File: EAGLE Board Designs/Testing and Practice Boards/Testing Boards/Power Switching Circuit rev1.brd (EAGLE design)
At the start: 93.2 x 66.3 mm, 50 parts, among them K1 J115F11A6*, Q1 SIR638ADP, Q2 SIR638ADP, Q3 SIR638ADP, Q4 SIR638ADP, U1 LTC4421, X1 CONNECTOR-3, X100 CONNECTOR-4AUTOSPORT, X101 CONNECTOR-4AUTOSPORT

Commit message: Add files via upload
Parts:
- Q1, Q2, Q3, Q4: device HyTechDevices:SO-8-POWERPAK -> HyTechDevices:POWERPAK_SO-8
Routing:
- net DCDC: track 43.7 -> 39.7 mm, vias 1 -> 0
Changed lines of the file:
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@@
 <drawing>
 <settings>
-<setting alwaysvectorfont="no"/>
+<setting alwaysvectorfont="yes"/>
 <setting verticaltext="up"/>
 </settings>
@@
 Power Switching Board rev1
 By: Sathya Gummadi</text>
-<text x="-15.748" y="32.131" size="0.9144" layer="21" font="vector" ratio="18">DCDC</text>
+<text x="-17.272" y="29.337" size="0.9144" layer="21" font="vector" ratio="18">DCDC</text>
 <text x="53.721" y="25.654" size="0.9144" layer="21" font="vector" ratio="18">GLVB</text>
 <text x="46.101" y="31.623" size="0.9144" layer="21" font="vector" ratio="18">OUT</text>
@@
 <attribute name="NAME" x="39.116" y="9.652" size="0.762" layer="21" font="vector"/>
 </element>
-<element name="Q4" library="HyTechDevices" package="SO-8-POWERPAK" value="SIR638ADP" x="29.718" y="-6.604" smashed="yes" rot="R270">
+<element name="Q4" library="HyTechDevices" package="POWERPAK_SO-8" value="SIR638ADP" x="29.718" y="-6.604" smashed="yes" rot="R270">
+<attribute name="MPN" value="SIR638ADP" x="29.718" y="-6.604" size="1.778" layer="27" rot="R270" display="off"/>
 <attribute name="NAME" x="32.385" y="-6.731" size="0.8128" layer="25" font="vector" rot="R270" align="bottom-center"/>
 </element>
-<element name="Q3" library="HyTechDevices" package="SO-8-POWERPAK" value="SIR638ADP" x="30.734" y="1.524" smashed="yes" rot="R90">
+<element name="Q3" library="HyTechDevices" package="POWERPAK_SO-8" value="SIR638ADP" x="30.734" y="1.524" smashed="yes" rot="R90">
+<attribute name="MPN" value="SIR638ADP" x="30.734" y="1.524" size="1.778" layer="27" rot="R90" display="off"/>
 <attribute name="NAME" x="24.638" y="1.524" size="0.762" layer="25" font="vector" rot="R90" align="bottom-center"/>
 </element>
-<element name="Q1" library="HyTechDevices" package="SO-8-POWERPAK" value="SIR638ADP" x="-3.048" y="25.273" smashed="yes" rot="R180">
-<attribute name="NAME" x="-3.048" y="29.591" size="0.762" layer="25" font="vector" rot="R180" align="bottom-center"/>
-</element>
-<element name="Q2" library="HyTechDevices" package="SO-8-POWERPAK" value="SIR638ADP" x="4.699" y="24.384" smashed="yes">
+<element name="Q1" library="HyTechDevices" package="POWERPAK_SO-8" value="SIR638ADP" x="-3.048" y="25.273" smashed="yes" rot="R180">
+<attribute name="MPN" value="SIR638ADP" x="-3.048" y="25.273" size="1.778" layer="27" rot="R180" display="off"/>
+<attribute name="NAME" x="-3.048" y="30.099" size="0.762" layer="25" font="vector" rot="R180" align="bottom-center"/>
+</element>
+<element name="Q2" library="HyTechDevices" package="POWERPAK_SO-8" value="SIR638ADP" x="4.699" y="24.384" smashed="yes">
+<attribute name="MPN" value="SIR638ADP" x="4.699" y="24.384" size="1.778" layer="27" display="off"/>
 <attribute name="NAME" x="2.667" y="27.686" size="0.762" layer="25" font="vector" align="bottom-center"/>
 </element>
@@
 <contactref element="K1" pad="CONTACT1"/>
 <polygon width="0.1524" layer="1" orphans="yes" thermals="no">
-<vertex x="44.577" y="21.844"/>
-<vertex x="50.673" y="26.797"/>
-<vertex x="53.34" y="26.797"/>
-<vertex x="53.34" y="11.049"/>
-<vertex x="60.071" y="-3.937" curve="-163.432311"/>
-<vertex x="54.220009375" y="-7.66035625"/>
-<vertex x="45.105534375" y="10.5686"/>
+<vertex x="44.45" y="21.59"/>
+<vertex x="50.8" y="26.67" curve="-133.114058"/>
+<vertex x="52.959" y="25.527"/>
+<vertex x="52.959" y="13.843"/>
+<vertex x="59.436" y="-3.683" curve="-176.962356"/>
+<vertex x="53.721" y="-5.969"/>
+<vertex x="42.418" y="15.748" curve="-79.752562"/>
+<vertex x="43.561" y="20.955" curve="-4.410509"/>
 </polygon>
 </signal>
@@
 <contactref element="D1" pad="3"/>
 <wire x1="-9.144" y1="21.908628125" x2="-9.144" y2="16.51" width="1.016" layer="1"/>
-<wire x1="-9.144" y1="21.908628125" x2="-12.49219375" y2="21.908628125" width="1.016" layer="16"/>
-<wire x1="-12.49219375" y1="21.908628125" x2="-12.5897625" y2="22.3659625" width="1.016" layer="16"/>
 <wire x1="-4.826" y1="15.884" x2="-8.518" y2="15.884" width="1.016" layer="1"/>
 <wire x1="-8.518" y1="15.884" x2="-9.144" y2="16.51" width="1.016" layer="1"/>
@@
 <wire x1="5.56790625" y1="11.595146875" x2="5.56790625" y2="11.91790625" width="0.4064" layer="1"/>
 <wire x1="5.56790625" y1="11.91790625" x2="6.223" y2="12.573" width="0.4064" layer="1"/>
-<wire x1="-3.8608" y1="25.4" x2="-3.8608" y2="22.6568" width="0.4064" layer="1"/>
+<wire x1="-3.7338" y1="25.273" x2="-3.8608" y2="22.6568" width="0.4064" layer="1"/>
 <wire x1="-3.8608" y1="22.6568" x2="6.223" y2="12.573" width="0.4064" layer="1"/>
 <wire x1="-9.144" y1="16.51" x2="-9.144" y2="13.1953" width="1.016" layer="1"/>
-<via x="-9.144" y="21.908628125" extent="1-16" drill="0.35"/>
 <contactref element="X101" pad="1"/>
 <polygon width="0.1524" layer="1" orphans="yes" thermals="no">
@@
 <vertex x="36.576" y="16.764"/>
 <vertex x="48.253365625" y="26.126934375" curve="137.037485"/>
-<vertex x="46.744759375" y="30.988"/>
-<vertex x="19.304" y="30.988"/>
+<vertex x="46.784171875" y="30.861"/>
 </polygon>
 </signal>
@@
 <contactref element="Q3" pad="4"/>
 <contactref element="U1" pad="31"/>
-<wire x1="32.766" y1="-1.016" x2="33.02" y2="-1.27" width="0.4064" layer="1"/>
+<wire x1="32.639" y1="-1.143" x2="33.02" y2="-1.27" width="0.4064" layer="1"/>
 <wire x1="33.02" y1="-1.27" x2="33.02" y2="-2.413" width="0.4064" layer="1"/>
 <via x="33.02" y="-2.413" extent="1-16" drill="0.35"/>
@@
 <via x="26.67" y="-3.302" extent="1-16" drill="0.35"/>
 <wire x1="26.67" y1="-3.302" x2="27.432" y2="-4.064" width="0.4064" layer="1"/>
-<wire x1="27.432" y1="-4.064" x2="27.686" y2="-4.064" width="0.4064" layer="1"/>
+<wire x1="27.432" y1="-4.064" x2="27.813" y2="-3.937" width="0.4064" layer="1"/>
 <wire x1="32.639" y1="-2.794" x2="27.178" y2="-2.794" width="0.4064" layer="16"/>
 <wire x1="26.67" y1="-3.302" x2="25.6708625" y2="-3.302" width="0.4064" layer="1"/>
@@
 </polygon>
 <wire x1="13.725771875" y1="4.3808" x2="14.61005625" y2="3.496515625" width="0.4064" layer="1"/>
-<wire x1="25.789028125" y1="-1.016" x2="30.226" y2="-1.016" width="0.4064" layer="1"/>
+<wire x1="25.789028125" y1="-1.016" x2="30.099" y2="-1.143" width="0.4064" layer="1"/>
 <wire x1="14.61005625" y1="3.496515625" x2="21.072275" y2="3.496515625" width="0.4064" layer="1"/>
 <wire x1="21.072275" y1="3.496515625" x2="21.17439375" y2="3.598634375" width="0.4064" layer="1"/>
@@
 <vertex x="26.924" y="-11.684"/>
 </polygon>
-<wire x1="29.591" y1="-7.4168" x2="27.9318" y2="-9.076" width="1.016" layer="1"/>
+<wire x1="29.718" y1="-7.2898" x2="27.9318" y2="-9.076" width="1.016" layer="1"/>
 <wire x1="24.13" y1="-8.246" x2="29.836" y2="-8.246" width="1.016" layer="1"/>
 <wire x1="29.836" y1="-8.246" x2="30.48" y2="-8.89" width="1.016" layer="1"/>
@@
 <wire x1="7.493" y1="13.8598625" x2="6.460553125" y2="14.892309375" width="0.4064" layer="1"/>
 <wire x1="7.493" y1="9.694334375" x2="7.493" y2="13.8598625" width="0.4064" layer="1"/>
-<wire x1="-0.508" y1="27.305" x2="0.762" y2="27.305" width="0.4064" layer="1"/>
-<via x="0.762" y="27.305" extent="1-16" drill="0.35"/>
-<wire x1="0.762" y1="27.305" x2="1.397" y2="26.67" width="0.4064" layer="16"/>
-<wire x1="1.397" y1="26.67" x2="1.397" y2="21.844" width="0.4064" layer="16"/>
+<via x="0.889" y="27.432" extent="1-16" drill="0.35"/>
+<wire x1="0.889" y1="27.432" x2="1.397" y2="26.924" width="0.4064" layer="16"/>
+<wire x1="1.397" y1="26.924" x2="1.397" y2="21.844" width="0.4064" layer="16"/>
 <wire x1="2.032" y1="21.209" x2="2.032" y2="20.828" width="0.4064" layer="16"/>
 <wire x1="2.032" y1="21.209" x2="1.397" y2="21.844" width="0.4064" layer="16"/>
@@
 <wire x1="2.54" y1="18.923" x2="6.460553125" y2="15.002446875" width="0.4064" layer="1"/>
 <wire x1="6.460553125" y1="15.002446875" x2="6.460553125" y2="14.892309375" width="0.4064" layer="1"/>
-<wire x1="2.159" y1="22.352" x2="2.159" y2="20.955" width="0.4064" layer="1"/>
-<wire x1="2.159" y1="20.955" x2="2.032" y2="20.828" width="0.4064" layer="1"/>
+<wire x1="2.032" y1="20.828" x2="2.032" y2="22.479" width="0.4064" layer="1"/>
+<wire x1="-0.381" y1="27.178" x2="-0.127" y2="27.432" width="0.4064" layer="1"/>
+<wire x1="-0.127" y1="27.432" x2="0.889" y2="27.432" width="0.4064" layer="1"/>
 </signal>
 <signal name="SOURCE1">

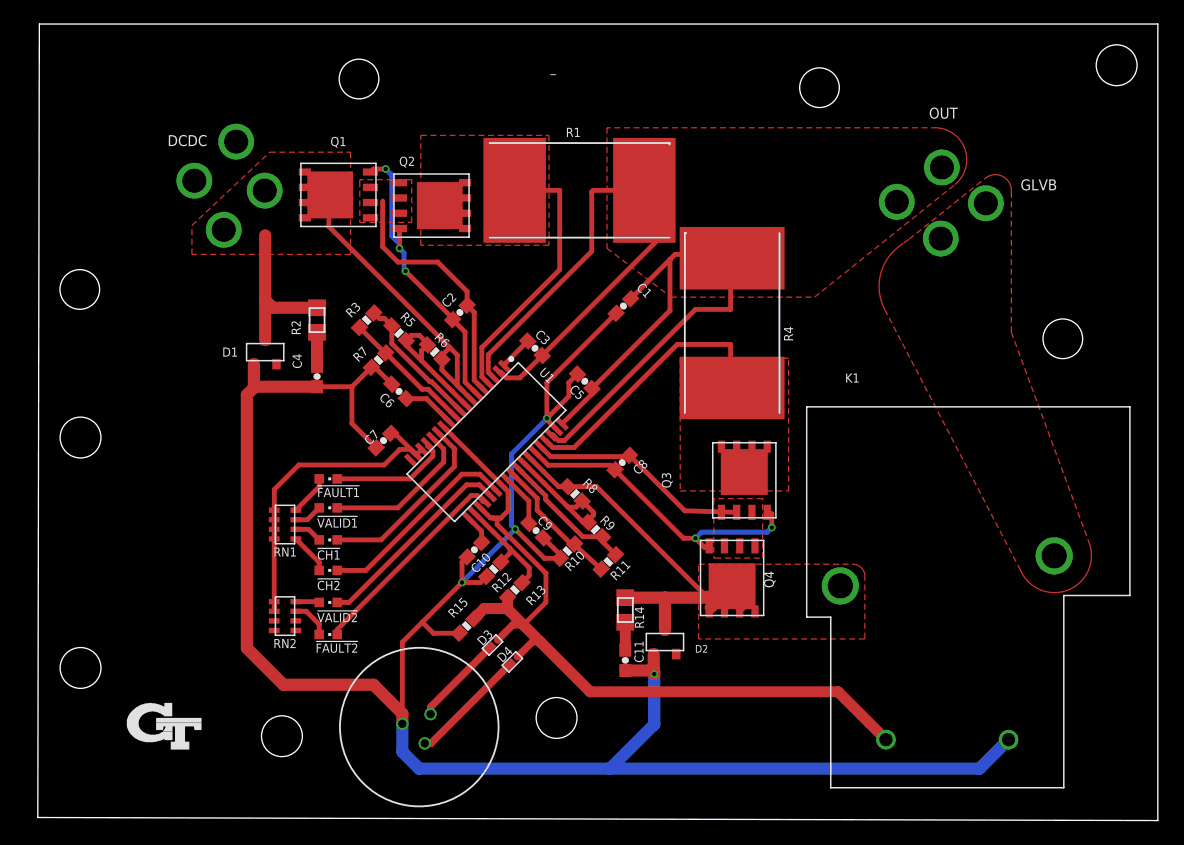
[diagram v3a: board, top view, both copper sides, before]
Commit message: Cleaned up silkscreen
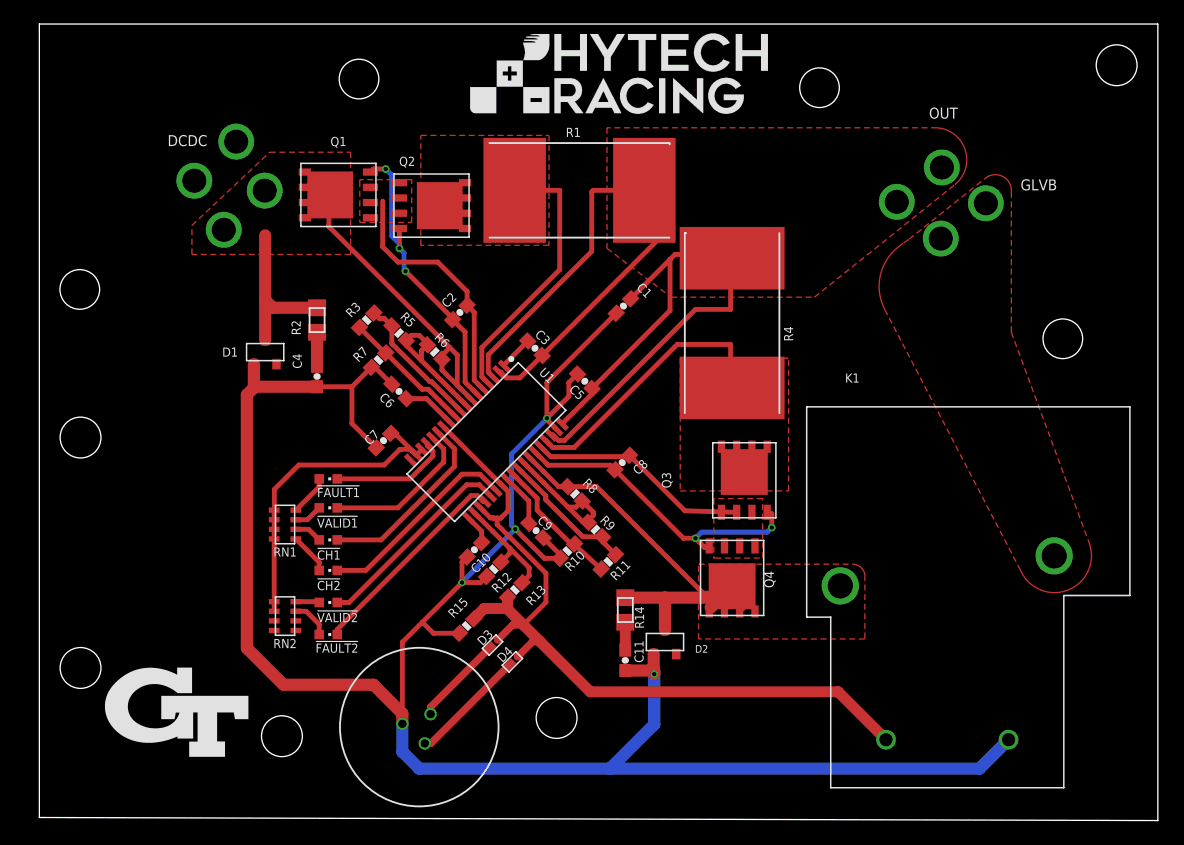
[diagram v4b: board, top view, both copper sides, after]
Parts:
- added U$5: (no value), HyTechAesthetics:LOGO_GT_0.50"
- added U$6: (no value), HyTechAesthetics:LOGO_HYTECH_1.0"
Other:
- board size 93.2 x 66.3 mm -> 93.1 x 66.3 mm
- board text added: "HyTech Racing 2021 Power Switching Board rev1 Designed by Sathya Gummadi"
- board text removed: "HyTech Racing 2021 Power Switching Board rev1 By: Sathya Gummadi"

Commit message: Layer fix
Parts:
- moved U$1 0.13 mm to (-24.5, -14.0)
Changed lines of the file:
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@@
 <drawing>
 <settings>
-<setting alwaysvectorfont="no"/>
+<setting alwaysvectorfont="yes"/>
 <setting verticaltext="up"/>
 </settings>
@@
 <text x="-4.826" y="-10.287" size="0.762" layer="21" font="vector">!VALID2</text>
 <text x="-4.826" y="-2.413" size="0.762" layer="21" font="vector">!VALID1</text>
-<text x="-17.145" y="-25.908" size="1.016" layer="51" font="vector" align="bottom-center">HyTech Racing 2021
+<text x="-17.145" y="-25.908" size="1.016" layer="21" font="vector" align="bottom-center">HyTech Racing 2021
 Power Switching Board rev1
 Designed by Sathya Gummadi</text>
@@
 <attribute name="VOLTAGE" value="" x="-7.493" y="-9.779" size="1.778" layer="27" rot="R90" display="off"/>
 </element>
-<element name="U$1" library="HyTechDevices" package="MOUNTING_M3" value="" x="-24.511" y="-14.097" smashed="yes"/>
+<element name="U$1" library="HyTechDevices" package="MOUNTING_M3" value="" x="-24.511" y="-13.97" smashed="yes"/>
 <element name="U$3" library="HyTechDevices" package="MOUNTING_M3" value="" x="-24.511" y="5.08" smashed="yes"/>
 <element name="U$4" library="HyTechDevices" package="MOUNTING_M3" value="" x="61.722" y="36.068" smashed="yes"/>

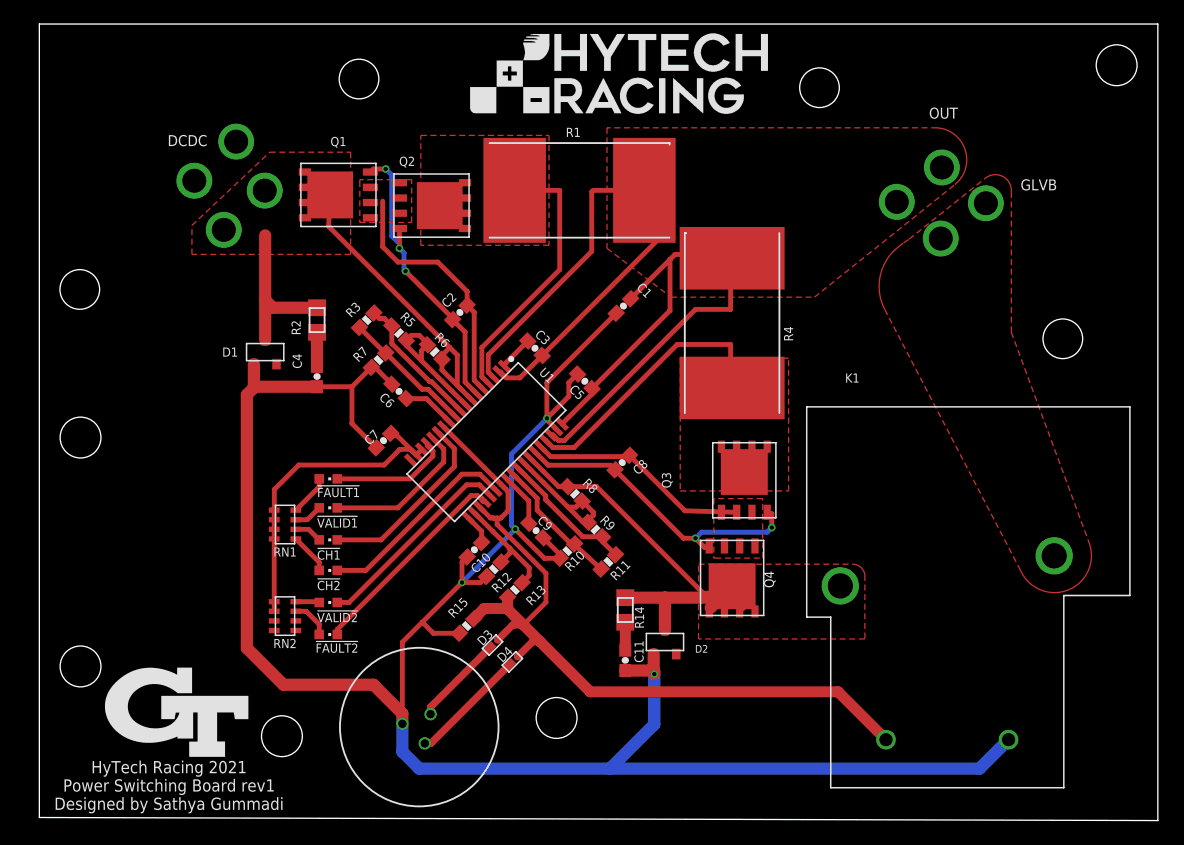
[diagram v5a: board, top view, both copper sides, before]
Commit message: Hopefully made changes to resolve JLC issue
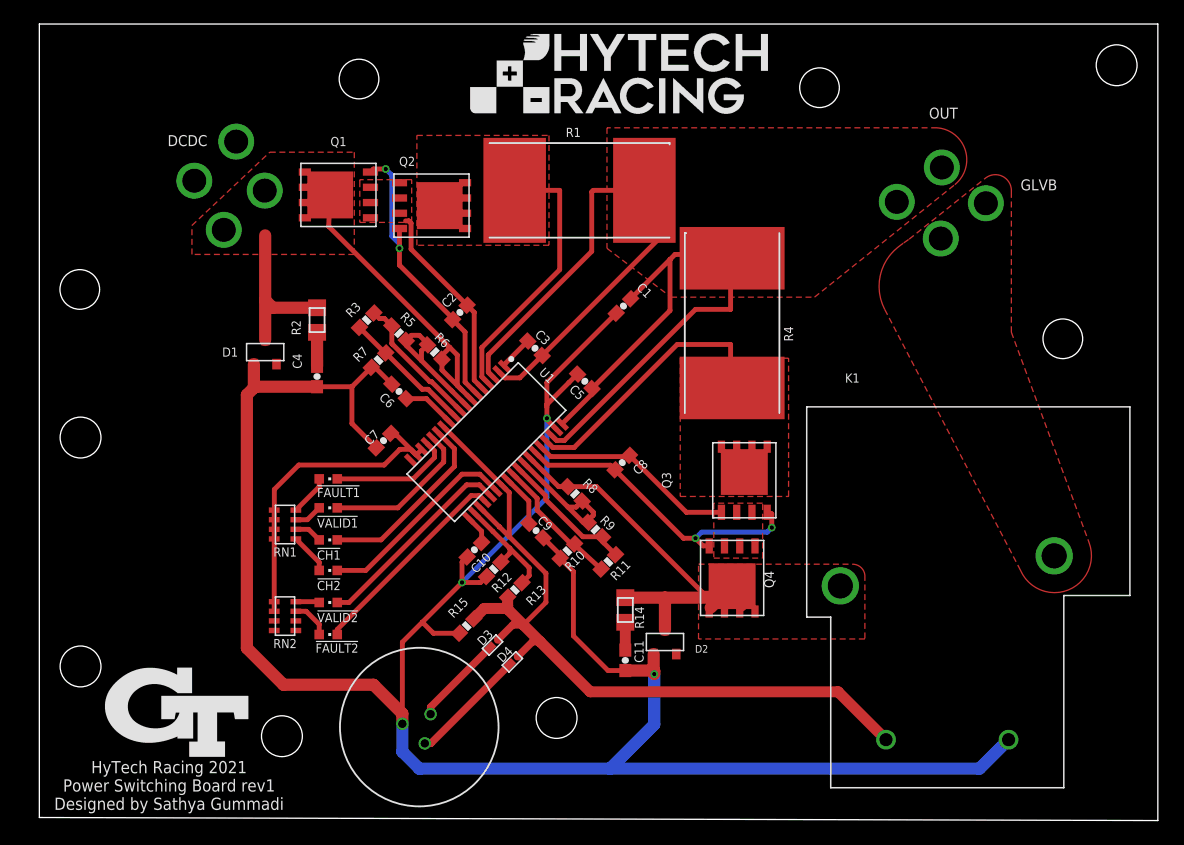
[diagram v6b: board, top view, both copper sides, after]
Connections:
- net CASIN renamed INTVDD
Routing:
- net GND: track 189.3 -> 195.6 mm, vias 4 -> 3
- net SOURCE1: track 21.0 -> 16.8 mm
- net SOURCE2: track 18.7 -> 17.5 mm
- net !SHDN: track 68.9 -> 69.6 mm
- net GATE1: track 25.0 -> 24.9 mm, vias 3 -> 2

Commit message: Resolved issues with power switching connectors
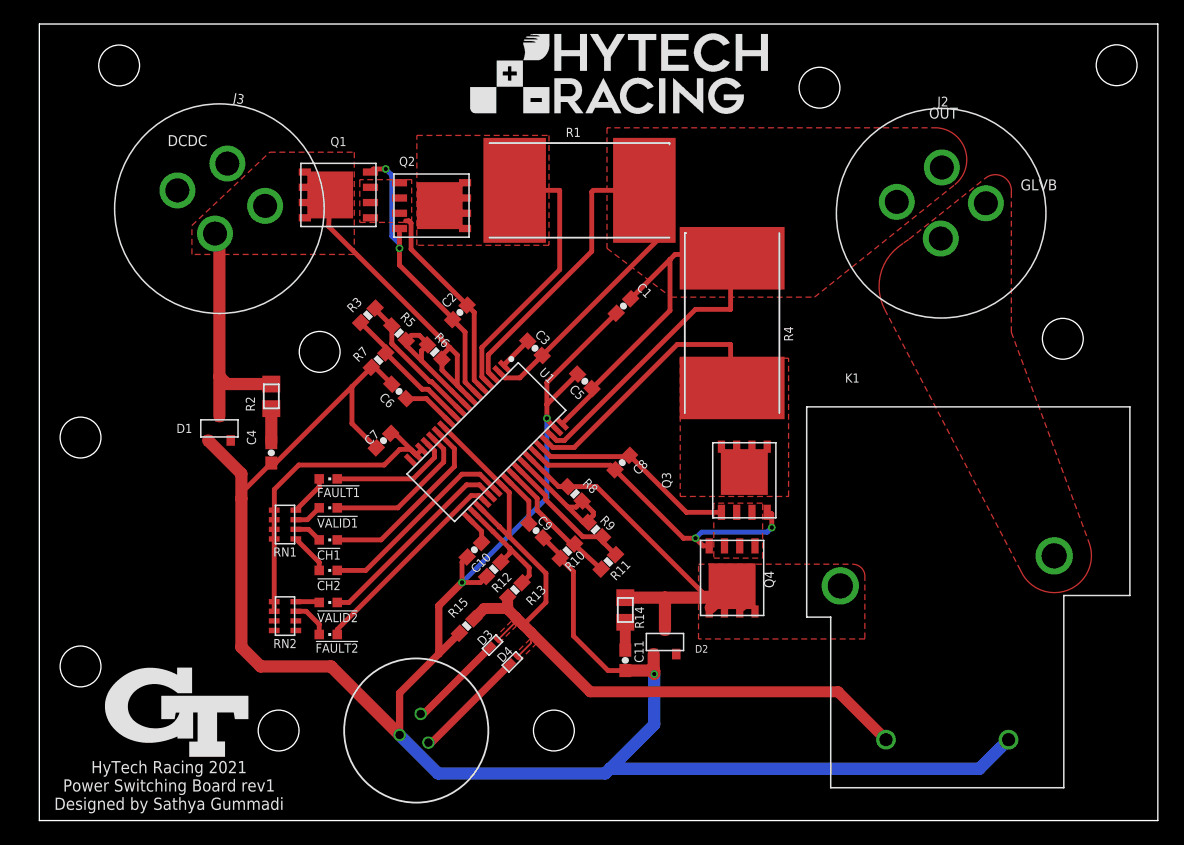
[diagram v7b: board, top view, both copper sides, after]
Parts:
- removed X1: CONNECTOR-3, HyTechDevices:AUTOSPORT_04-35
- removed X100, X101: CONNECTOR-4AUTOSPORT, HyTechDevices:AUTOSPORT_12-04
- added J1: CONNECTOR-3_, HyTechDevices:SOURIAU_04-35
- added J2, J3: CONNECTOR-4_SOURIAU_, HyTechDevices:SOURIAU_12-04
- moved D1 7.41 mm to (-13.0, 5.84)
- moved C4 7.41 mm to (-8.64, 3.81)
- moved R2 7.41 mm to (-8.64, 8.51)
- moved R3 0.42 mm to (-0.60, 15.3)
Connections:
- net !SHDN renamed !SHDN!
- net DCDC: now also J3.3, J3.4; no longer X101.1, X101.4
- net GLVB: now also J2.3, J2.4; no longer X100.3, X100.4
- net GND: now also J1.A; no longer X1.A
- net OUT: now also J2.1, J2.2; no longer X100.1, X100.2
- net RIGHT_BRB: now also D4.1, J1.B; no longer D3.1, X1.B
- net START: now also D3.1, J1.C; no longer D4.1, X1.C
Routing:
- net DCDC: track 39.7 -> 46.4 mm
- net RIGHT_BRB: track 7.59 -> 9.48 mm
- net START: track 9.81 -> 8.06 mm
- net GND: track 195.6 -> 194.1 mm
- added copper zone on layer 1, net !SHDN!
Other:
- outline, holes or cut-outs redrawn
